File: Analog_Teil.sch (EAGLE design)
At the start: 32 parts, among them IC1 OPA388, IC2 INA828ID, IC3 OPA388, IC4 OPA388, IC5 OPA388, IC6 OPA388, IC7 OPA388

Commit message: Noch ein Test
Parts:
- added R16, R17: 6.8k, rcl:R-EU_R0805
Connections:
- new net N$16: R16.2, R17.1
- net N$21: now also R16.1
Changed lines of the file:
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@@
 <part name="C9" library="rcl" library_urn="urn:adsk.eagle:library:334" deviceset="C-EU" device="C0805" package3d_urn="urn:adsk.eagle:package:23617/2" value="4.7n"/>
 <part name="C10" library="rcl" library_urn="urn:adsk.eagle:library:334" deviceset="C-EU" device="C0805" package3d_urn="urn:adsk.eagle:package:23617/2" value="470n"/>
+<part name="R16" library="rcl" library_urn="urn:adsk.eagle:library:334" deviceset="R-EU_" device="R0805" package3d_urn="urn:adsk.eagle:package:23553/2" value="6.8k"/>
+<part name="R17" library="rcl" library_urn="urn:adsk.eagle:library:334" deviceset="R-EU_" device="R0805" package3d_urn="urn:adsk.eagle:package:23553/2" value="6.8k"/>
 </parts>
 <sheets>
@@
 <attribute name="NAME" x="200.279" y="199.644" size="1.778" layer="95" rot="R90"/>
 <attribute name="VALUE" x="205.359" y="199.644" size="1.778" layer="96" rot="R90"/>
+</instance>
+<instance part="R16" gate="G$1" x="281.94" y="190.5" smashed="yes">
+<attribute name="NAME" x="278.13" y="191.9986" size="1.778" layer="95"/>
+<attribute name="VALUE" x="278.13" y="187.198" size="1.778" layer="96"/>
+</instance>
+<instance part="R17" gate="G$1" x="292.1" y="190.5" smashed="yes">
+<attribute name="NAME" x="288.29" y="191.9986" size="1.778" layer="95"/>
+<attribute name="VALUE" x="288.29" y="187.198" size="1.778" layer="96"/>
 </instance>
 </instances>
@@
 <wire x1="261.62" y1="190.5" x2="276.86" y2="190.5" width="0.1524" layer="91"/>
 <junction x="261.62" y="190.5"/>
+<pinref part="R16" gate="G$1" pin="1"/>
 </segment>
 </net>
@@
 </segment>
 </net>
+<net name="N$16" class="0">
+<segment>
+<pinref part="R16" gate="G$1" pin="2"/>
+<pinref part="R17" gate="G$1" pin="1"/>
+</segment>
+</net>

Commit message: Erweiterungen am Schaltplan
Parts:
- removed R16, R17: 6.8k, rcl:R-EU_R0805
- added C11, C12, C13, C14, C15, C16, C17, C18, C19, C20, C21, C22, C23, C24: 100n, rcl:C-EUC0805
- added JP1: (no value), jumper:JP3Q
- added JP2: (no value), jumper:JP1Q
- added JP3: (no value), jumper:JP2E
- added JP4: (no value), jumper:JP2Q
- added R18, R19: 500k, rcl:R-EU_R0805
- added TP1: TPPAD1-13, testpad:TPPAD1-13
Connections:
- removed net N$16: R16.2, R17.1
- new net N$23: IC2.-IN, R19.2
- new net N$24: IC2.+IN, R18.2
- new net N$25: R18.1, R19.1
- new net N$26: C11.1, IC2.-VS
- new net N$27: C12.2, IC2.+VS
- new net N$28: C14.2, IC1.V-
- new net N$29: C13.1, IC1.V+
- new net N$30: C16.2, IC3.V-
- new net N$31: C15.1, IC3.V+
- new net N$32: C18.2, IC4.V-
- new net N$33: C17.1, IC4.V+
- new net N$34: C20.2, IC5.V-
- new net N$35: C19.1, IC5.V+
- new net N$36: C22.2, IC6.V-
- new net N$37: C21.1, IC6.V+
- new net N$38: C24.2, IC7.V-
- new net N$39: C23.1, IC7.V+
- net GND1: now also C11.2, C12.1, C13.2, C14.1, C15.2, C16.1, C17.2, C18.1, C19.2, C20.1, C21.2, C22.1, C23.2, C24.1
- net N$21: no longer R16.1

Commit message: Nächste Erweiterung
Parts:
- added C25, C26, C27, C28, C29, C30: 10p, rcl:C-EUC0805
- added JP10, JP11, JP7, JP8, JP9: (no value), jumper:JP3Q
- added JP5, JP6: (no value), jumper:JP2Q
- added R16: 50k, pot:TRIM_EU-SM-42/43W
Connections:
- removed net N$13: C6.2, IC4.IN-, IC4.OUT, R8.1
- new net N$16: JP5.4, R1.1
- new net N$40: JP5.2, R16.A
- new net N$41: JP7.1, JP7.6, R18.1
- new net N$42: C1.1, JP10.5, JP11.5, JP8.5
- new net N$43: JP11.1
- new net N$44: JP9.5
- new net N$45: JP11.3, JP8.3, JP9.3, R6.1
- new net N$46: JP10.3
- new net N$47: C30.2
- new net N$49: C10.1, JP10.1, JP8.1, JP9.1, R11.1, R14.1
- new net N$53: C28.1, C28.2, C6.2, IC4.IN-, IC4.OUT, R8.1
- net GND1: now also JP7.3, JP7.5
- net N$1: now also JP5.1, JP5.3; no longer R1.1
- net N$10: now also C29.1, C29.2, JP9.2, JP9.4, JP9.6; no longer R6.1
- net N$15: now also C27.1, C27.2, JP10.2, JP10.4, JP10.6; no longer C10.1, R11.1, R14.1
- net N$18: now also C25.2
- net N$19: now also C26.2
- net N$2: now also R16.S
- net N$20: now also C25.1
- net N$21: now also C26.1, JP11.2, JP11.4, JP11.6
- net N$25: now also JP7.2, JP7.4; no longer R18.1
- net N$5: now also JP8.2, JP8.4, JP8.6; no longer C1.1
- net N$6: now also C30.1
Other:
- moved on the sheet: C1, C10, C13, C14, C15, C16, C17, C18, C19, C2, C20, C21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

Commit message: Nächste Bearbeitung
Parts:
- removed C11, C12, C13, C14, C15, C16, C17, C18, C19, C20, C21, C22, C23, C24: 100n, rcl:C-EUC0805
- removed C26, C27, C28, C29, C30: 10p, rcl:C-EUC0805
- removed JP1: (no value), jumper:JP3Q
- removed JP6: (no value), jumper:JP2Q
- removed R10: 138k, rcl:R-EU_R0805
- added C+1.5, C+3, C+9, C-1.5, C_-9: 100u, ECA-1HM101:ECA-1HM101
- added C_1+, C_1-, C_H11+, C_H11-, C_H12+, C_H12-, C_N11+, C_N11-, C_N12+, C_N12-, C_T11+, C_T11-, C_T12+, C_T12-: 100n, rcl:C-EUC0805
- added C_H11.0, C_H12.0, C_N11.0, C_T11.0, C_T12.0: 10p, rcl:C-EUC0805
- added R_N1.2: 138k, rcl:R-EU_R0805
- added TP2, TP3, TP4, TP5, TP6, TP7: TPPAD1-13, testpad:TPPAD1-13
- added X1, X2: (no value), con-wago:233-108
- R1: value 50k -> 200
- R16: value 50k -> 200; SPICEPREFIX (none) -> J
- R_RS+, R_RS-: value 500k -> 1Meg
- renumbered C1 to C_H11.1, C10 to C_N1.1, C2 to C_H11.2, C25 to C_N12.0, C3 to C_H12.1, C4 to C_H12.2, C5 to C_T11.2, C6 to C_T11.1, C7 to C_T12.2, C8 to C_T12.1, C9 to C_N1.2, IC1 to H11, IC2 to INA_1, IC3 to H12, IC4 to T11, IC5 to T12, IC6 to N11, IC7 to N12, R11 to R_N1.1, R12 to R_N1.3, R13 to R_N1.5, R14 to R_N1.6, R15 to R_N1.4, R18 to R_RS+, R19 to R_RS-, R2 to R_H11.1, R3 to R_H11.2, R4 to R_H12.1, R5 to R_H12.2, R6 to R_T11.1, R7 to R_T11.2, R8 to R_T12.1, R9 to R_T12.2
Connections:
- removed net GND1: C11.2, C12.1, C13.2, C14.1, C15.2, C16.1, C17.2, C18.1, C19.2, C20.1, C21.2, C22.1, C23.2, C24.1, INA_1.REF, JP7.3, JP7.5
- removed net N$10: C29.1, C29.2, H12.IN-, H12.OUT, JP9.2, JP9.4, JP9.6, R_H12.1.2
- removed net N$15: C27.1, C27.2, C_T12.1.2, JP10.2, JP10.4, JP10.6, T12.IN-, T12.OUT
- removed net N$21: C26.1, JP11.2, JP11.4, JP11.6, N11.OUT, R_N1.5.2
- removed net N$23: INA_1.-IN, R_RS-.2
- removed net N$24: INA_1.+IN, R_RS+.2
- removed net N$26: C11.1, INA_1.-VS
- removed net N$27: C12.2, INA_1.+VS
- removed net N$28: C14.2, H11.V-
- removed net N$29: C13.1, H11.V+
- removed net N$30: C16.2, H12.V-
- removed net N$31: C15.1, H12.V+
- removed net N$32: C18.2, T11.V-
- removed net N$33: C17.1, T11.V+
- removed net N$34: C20.2, T12.V-
- removed net N$35: C19.1, T12.V+
- removed net N$36: C22.2, N11.V-
- removed net N$37: C21.1, N11.V+
- removed net N$38: C24.2, N12.V-
- removed net N$39: C23.1, N12.V+
- removed net N$43: JP11.1
- removed net N$44: JP9.5
- removed net N$46: JP10.3
- removed net N$5: INA_1.OUT, JP8.2, JP8.4, JP8.6
- removed net N$6: C30.1, C_H12.1.1, H11.IN-, H11.OUT, R_H11.1.2
- new net +1.5V: C+1.5.+, C_H11+.1, C_H12+.1, C_N11+.1, C_N12+.1, C_T11+.1, C_T12+.1, H11.V+, H12.V+, N11.V+, N12.V+, T11.V+, T12.V+, X1.B-6
- new net +3V: C+3.+, X1.B-7
- new net +9V: C+9.+, C_1+.1, INA_1.+VS, X1.B-3
- new net -1.5V: C-1.5.-, C_H11-.2, C_H12-.2, C_N11-.2, C_N12-.2, C_T11-.2, C_T12-.2, H11.V-, H12.V-, N11.V-, N12.V-, T11.V-, T12.V-, X1.B-4
- new net -9V: C_-9.-, C_1-.1, INA_1.-VS, X1.B-1
- new net H1_ADC: JP9.5, TP5.TP
- new net H1_OUT: C_H12.0.1, C_H12.0.2, H12.IN-, H12.OUT, JP9.2, JP9.4, JP9.6, R_H12.1.2, TP2.TP
- new net INA1_OUT: INA_1.OUT, JP8.2, JP8.4, JP8.6, TP1.TP
- new net LS+: X2.B-4
- new net LS-: X2.B-5
- new net N$54: X2.B-6
- new net N$55: X1.B-8
- new net N$56: X2.B-7
- new net N$57: X2.B-8
- new net N1_ADC: JP11.1, TP7.TP
- new net N1_OUT: C_N11.0.1, JP11.2, JP11.4, JP11.6, N11.OUT, R_N1.5.2, TP4.TP
- new net REF: INA_1.REF, X2.B-3
- new net RS+: INA_1.+IN, R_RS+.2, X2.B-1
- new net RS-: INA_1.-IN, R_RS-.2, X2.B-2
- new net T1_ADC: JP10.3, TP6.TP
- new net T1_OUT: C_T12.0.1, C_T12.0.2, C_T12.1.2, JP10.2, JP10.4, JP10.6, T12.IN-, T12.OUT, TP3.TP
- net AGND: now also C+1.5.-, C+3.-, C+9.-, C-1.5.+, C_-9.+, C_1+.2, C_1-.2, C_H11+.2, C_H11-.1, C_H12+.2, C_H12-.1, C_N11+.2, C_N11-.1, C_N12+.2, C_N12-.1, C_T11+.2, C_T11-.1, C_T12+.2, C_T12-.1, JP7.3, JP7.5, R_N1.2.1, X1.B-2, X1.B-5
- net N$17: now also R_N1.2.2; no longer R10.2
- net N$19: now also C_N11.0.2; no longer C26.2
- net N$47: now also C_H11.0.1, C_H11.0.2, C_H12.1.1, H11.IN-, H11.OUT, R_H11.1.2; no longer C30.2
- net N$53: now also C_T11.0.1, C_T11.0.2; no longer C28.1, C28.2
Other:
- moved on the sheet: JP5, R1, R16, TP1

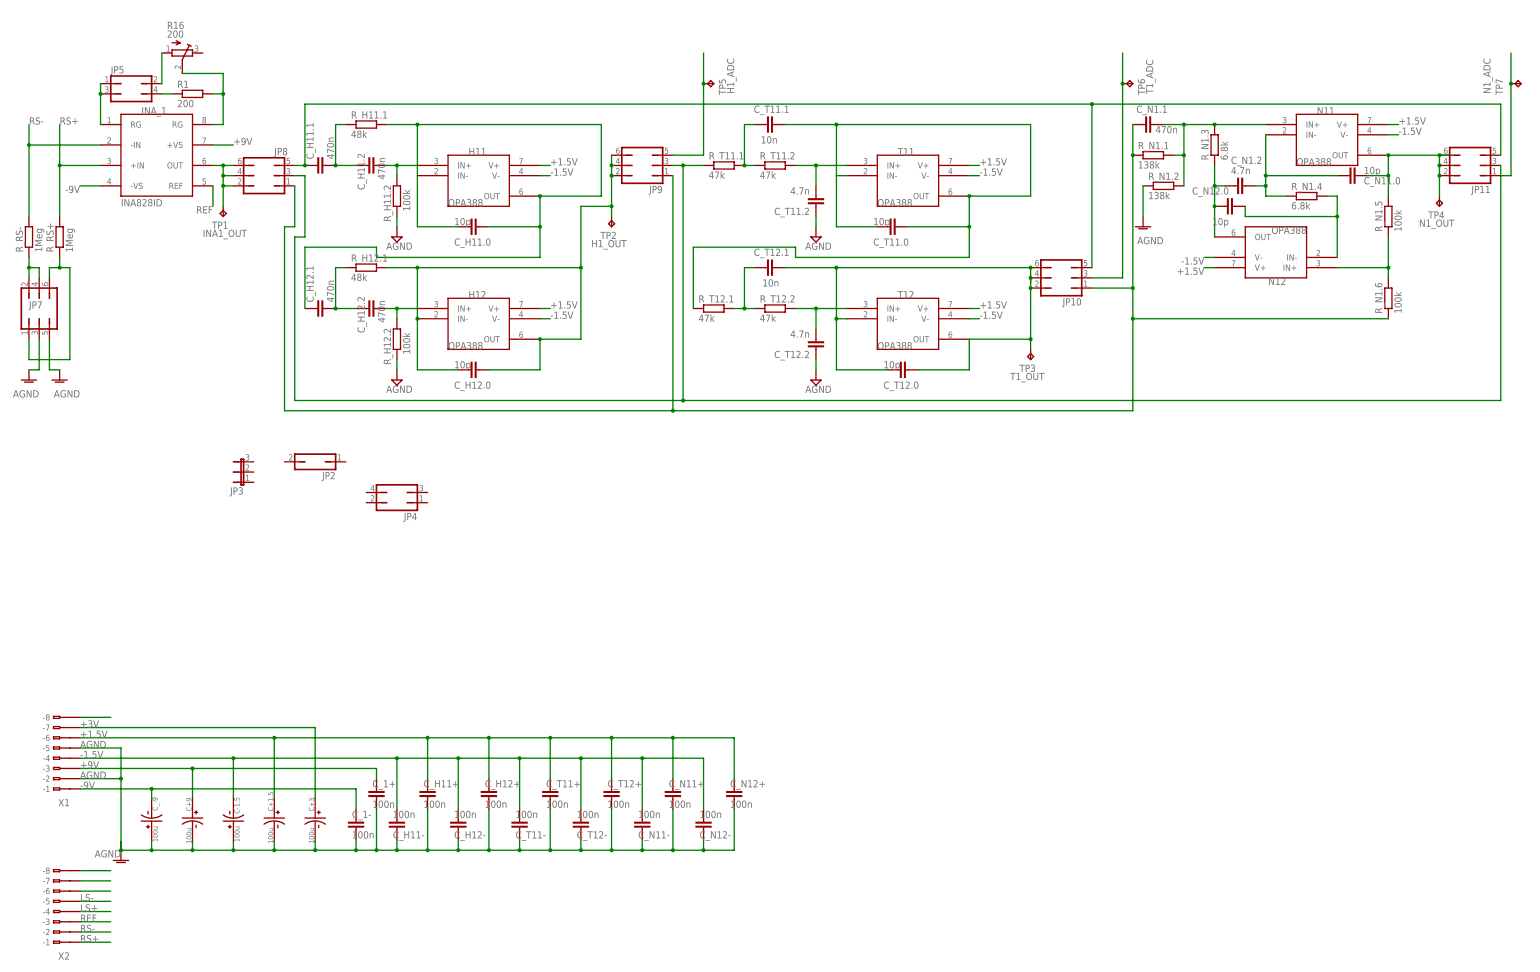
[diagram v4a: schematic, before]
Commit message: Überspannungsschutz hinzugefügt
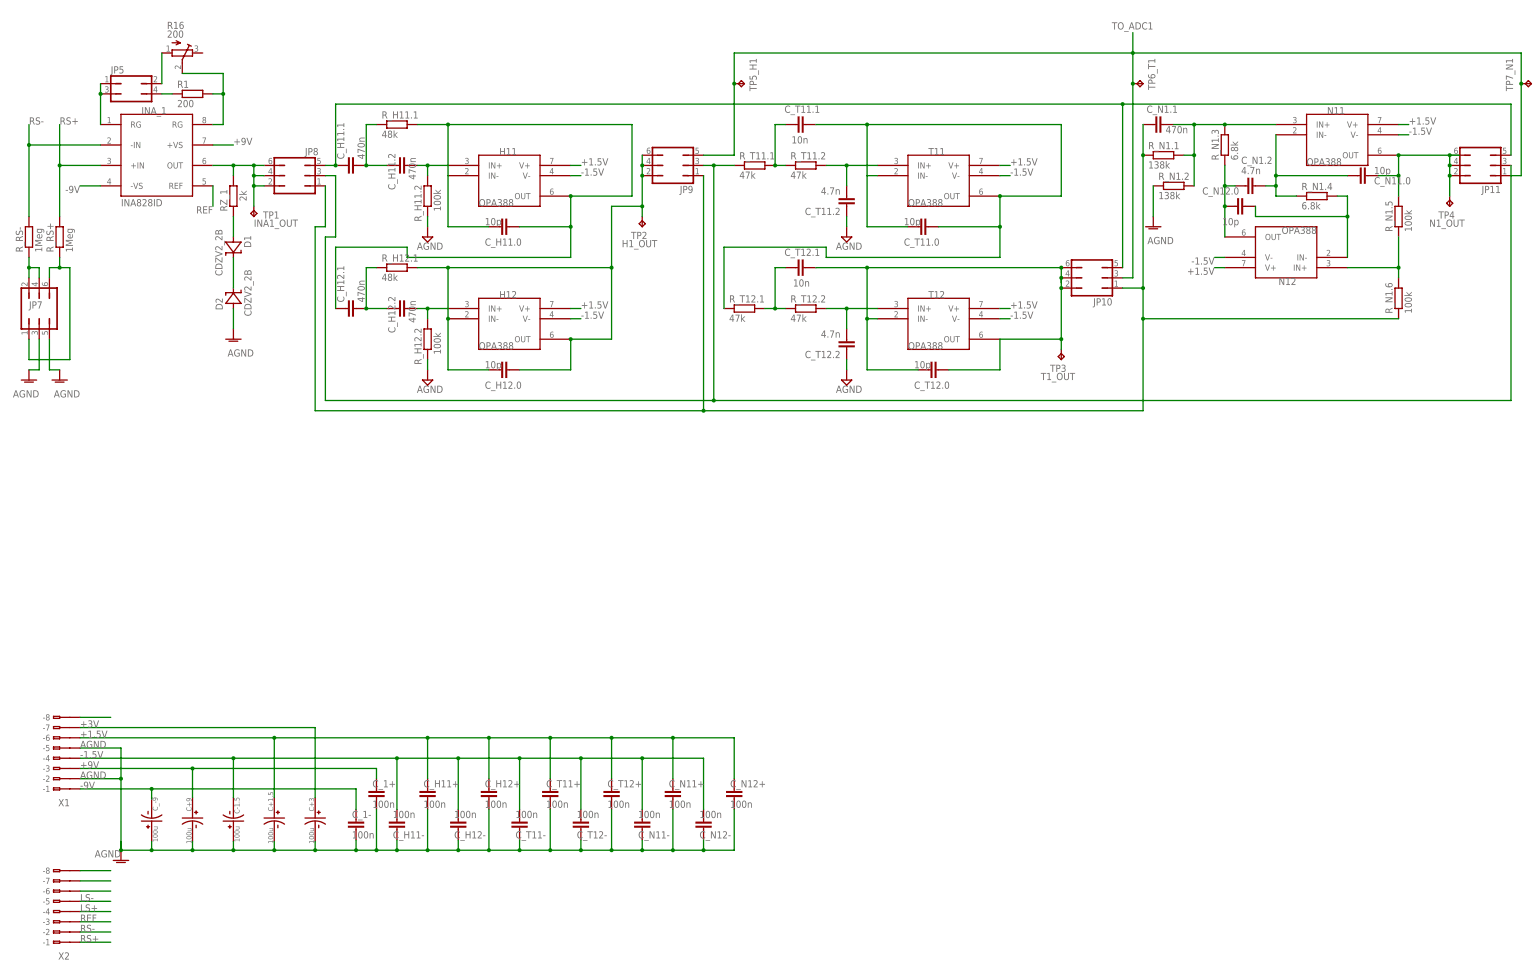
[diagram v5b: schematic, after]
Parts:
- removed JP2: (no value), jumper:JP1Q
- removed JP3: (no value), jumper:JP2E
- removed JP4: (no value), jumper:JP2Q
- removed TP5, TP6, TP7: TPPAD1-13, testpad:TPPAD1-13
- added D1, D2: CDZV2_2B, cdzv2_2b:CDZV2_2BSOD923
- added RZ_1: 2k, rcl:R-EU_R0805
- added TP5_H1, TP6_T1, TP7_N1: TPPAD1-13, testpad:TPPAD1-13
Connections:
- removed net H1_ADC: JP9.5, TP5.TP
- removed net N1_ADC: JP11.1, TP7.TP
- removed net T1_ADC: JP10.3, TP6.TP
- new net N$5: D1.A, RZ_1.1
- new net N$6: D1.C, D2.C
- new net TO_ADC1: JP10.3, JP11.1, JP9.5, TP5_H1.TP, TP6_T1.TP, TP7_N1.TP
- net AGND: now also D2.A
- net INA1_OUT: now also RZ_1.2
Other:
- moved on the sheet: C_H11.0, C_H11.1, C_H11.2, C_H12.0, C_H12.1, C_H12.2, C_N1.1, C_N1.2, C_N11.0, C_N12.0, C_T11.0, C_T11.1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
